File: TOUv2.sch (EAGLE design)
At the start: 9 parts, among them Q1 32.768KHz, U1 ATTINY85-20SU, U3 LIGHTSENSORALS

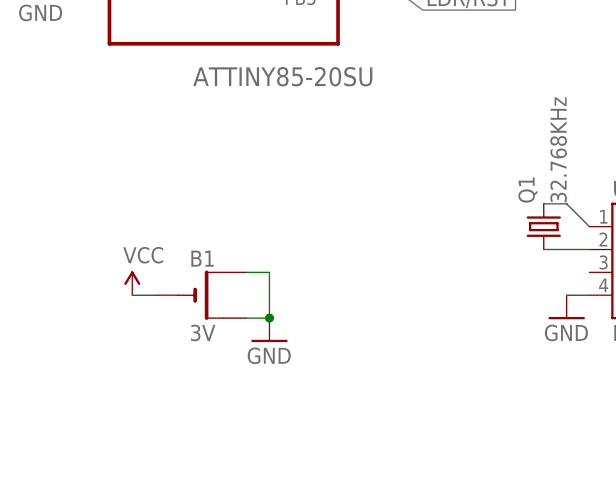
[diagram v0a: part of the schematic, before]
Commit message: Fix CR2032 error, simplify routing, add BOM
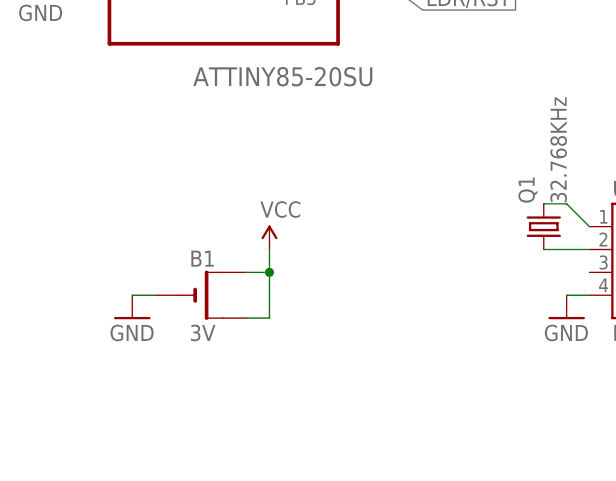
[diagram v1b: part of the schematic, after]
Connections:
- net GND: now also B1.-; no longer B1.+, B1.+1
- net VCC: now also B1.+, B1.+1; no longer B1.-
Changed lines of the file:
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@@
 <instance part="P+3" gate="1" x="83.82" y="71.12"/>
 <instance part="GND3" gate="1" x="83.82" y="53.34"/>
-<instance part="GND5" gate="1" x="27.94" y="20.32"/>
-<instance part="P+1" gate="1" x="12.7" y="25.4"/>
+<instance part="GND5" gate="1" x="12.7" y="22.86"/>
+<instance part="P+1" gate="1" x="27.94" y="30.48"/>
 <instance part="U$1" gate="G$1" x="73.66" y="30.48"/>
 <instance part="GND6" gate="1" x="60.96" y="22.86"/>
@@
 </segment>
 <segment>
-<pinref part="B1" gate="G$1" pin="+1"/>
-<wire x1="25.4" y1="22.86" x2="27.94" y2="22.86" width="0.1524" layer="91"/>
-<pinref part="GND5" gate="1" pin="GND"/>
-<pinref part="B1" gate="G$1" pin="+"/>
-<wire x1="25.4" y1="27.94" x2="27.94" y2="27.94" width="0.1524" layer="91"/>
-<wire x1="27.94" y1="27.94" x2="27.94" y2="22.86" width="0.1524" layer="91"/>
-<junction x="27.94" y="22.86"/>
-</segment>
-<segment>
 <pinref part="U$1" gate="G$1" pin="GND"/>
 <pinref part="GND6" gate="1" pin="GND"/>
 <wire x1="63.5" y1="25.4" x2="60.96" y2="25.4" width="0.1524" layer="91"/>
+</segment>
+<segment>
+<pinref part="B1" gate="G$1" pin="-"/>
+<pinref part="GND5" gate="1" pin="GND"/>
+<wire x1="15.24" y1="25.4" x2="12.7" y2="25.4" width="0.1524" layer="91"/>
 </segment>
 </net>
@@
 </segment>
 <segment>
-<pinref part="B1" gate="G$1" pin="-"/>
-<wire x1="15.24" y1="25.4" x2="12.7" y2="25.4" width="0.1524" layer="91"/>
-<pinref part="P+1" gate="1" pin="VCC"/>
-</segment>
-<segment>
 <pinref part="U$1" gate="G$1" pin="VCC"/>
 <pinref part="P+5" gate="1" pin="VCC"/>
 <wire x1="86.36" y1="33.02" x2="88.9" y2="33.02" width="0.1524" layer="91"/>
 </segment>
+<segment>
+<pinref part="B1" gate="G$1" pin="+1"/>
+<pinref part="P+1" gate="1" pin="VCC"/>
+<wire x1="25.4" y1="22.86" x2="27.94" y2="22.86" width="0.1524" layer="91"/>
+<wire x1="27.94" y1="22.86" x2="27.94" y2="27.94" width="0.1524" layer="91"/>
+<pinref part="B1" gate="G$1" pin="+"/>
+<wire x1="27.94" y1="27.94" x2="27.94" y2="30.48" width="0.1524" layer="91"/>
+<wire x1="25.4" y1="27.94" x2="27.94" y2="27.94" width="0.1524" layer="91"/>
+<junction x="27.94" y="27.94"/>
+</segment>
 </net>
